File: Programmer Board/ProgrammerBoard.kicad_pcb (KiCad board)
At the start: 2 copper layers, 9 parts

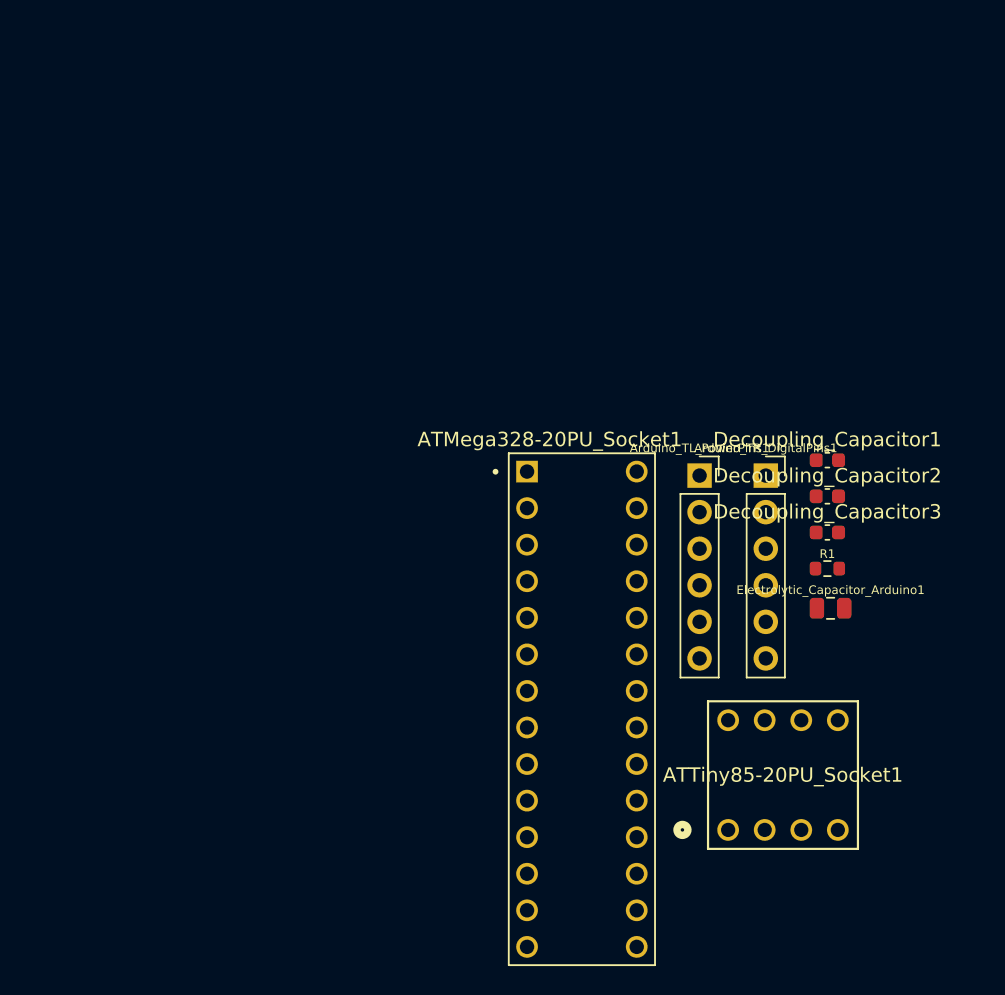
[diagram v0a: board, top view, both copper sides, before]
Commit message: Added Header Socket Pins 1x4, 1x6, 1x8
- For flush attachment to Arduino Uno R3
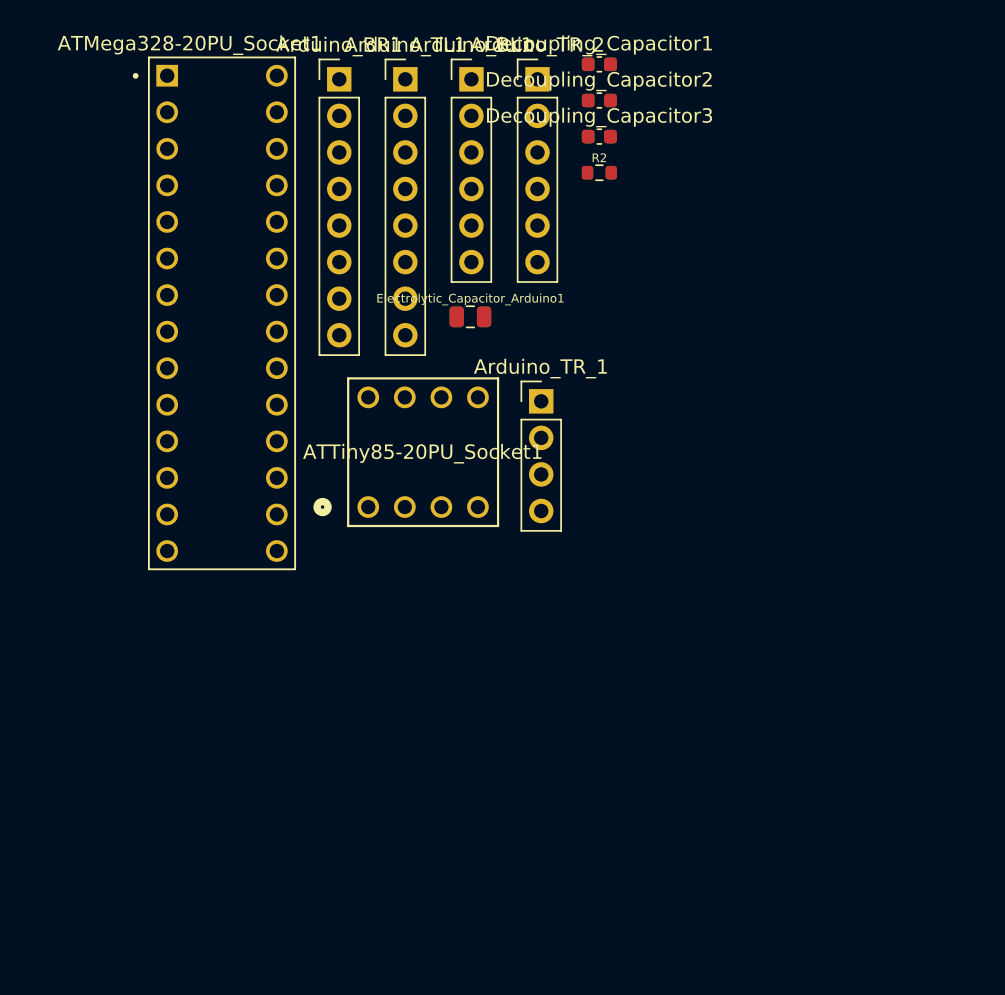
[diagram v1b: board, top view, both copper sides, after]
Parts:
- removed Arduino_TL_PowerPins1, Arduino_TR_DigitalPins1: Conn_01x06_Female, rsx_headers:PinSocket_1x06_P2.54mm_Vertical
- removed R1: 10k, rsx_resistors:R_0603_1608Metric
- added Arduino_BL1: header_1x6_arduino, Connector_PinHeader_2.54mm:PinHeader_1x06_P2.54mm_Vertical, F.Cu at (42.5, 19.8)
- added Arduino_BR1: header_1x8_arduino, Connector_PinHeader_2.54mm:PinHeader_1x08_P2.54mm_Vertical, F.Cu at (33.3, 19.8)
- added Arduino_TL1: header_1x8_arduino, Connector_PinHeader_2.54mm:PinHeader_1x08_P2.54mm_Vertical, F.Cu at (37.9, 19.8)
- added Arduino_TR_1: header_1x4_arduino, Connector_PinHeader_2.54mm:PinHeader_1x04_P2.54mm_Vertical, F.Cu at (47.4, 42.2)
- added Arduino_TR_2: header_1x6_arduino, Connector_PinHeader_2.54mm:PinHeader_1x06_P2.54mm_Vertical, F.Cu at (47.1, 19.8)
- added R2: 10k, rsx_resistors:R_0603_1608Metric, F.Cu at (51.4, 26.3)
- moved ATMega328-20PU_Socket1 37.2 mm to (25.2, 36.1)
- moved ATTiny85-20PU_Socket1 33.6 mm to (35.4, 49.5)
- moved Electrolytic_Capacitor_Arduino1 32.2 mm to (42.5, 36.3)
- moved Decoupling_Capacitor1 31.7 mm to (51.4, 18.8)
- moved Decoupling_Capacitor2 31.7 mm to (51.4, 21.3)
- moved Decoupling_Capacitor3 31.7 mm to (51.4, 23.8)
